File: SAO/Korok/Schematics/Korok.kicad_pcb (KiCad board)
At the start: 2 copper layers, 44.5 x 76.5 mm, 7 parts, among them J2 Debug, J3 Conn_02x03_Odd_Even, SW1 SW_SPDT, U1 CH32V006, U4 W25Q16JVSS

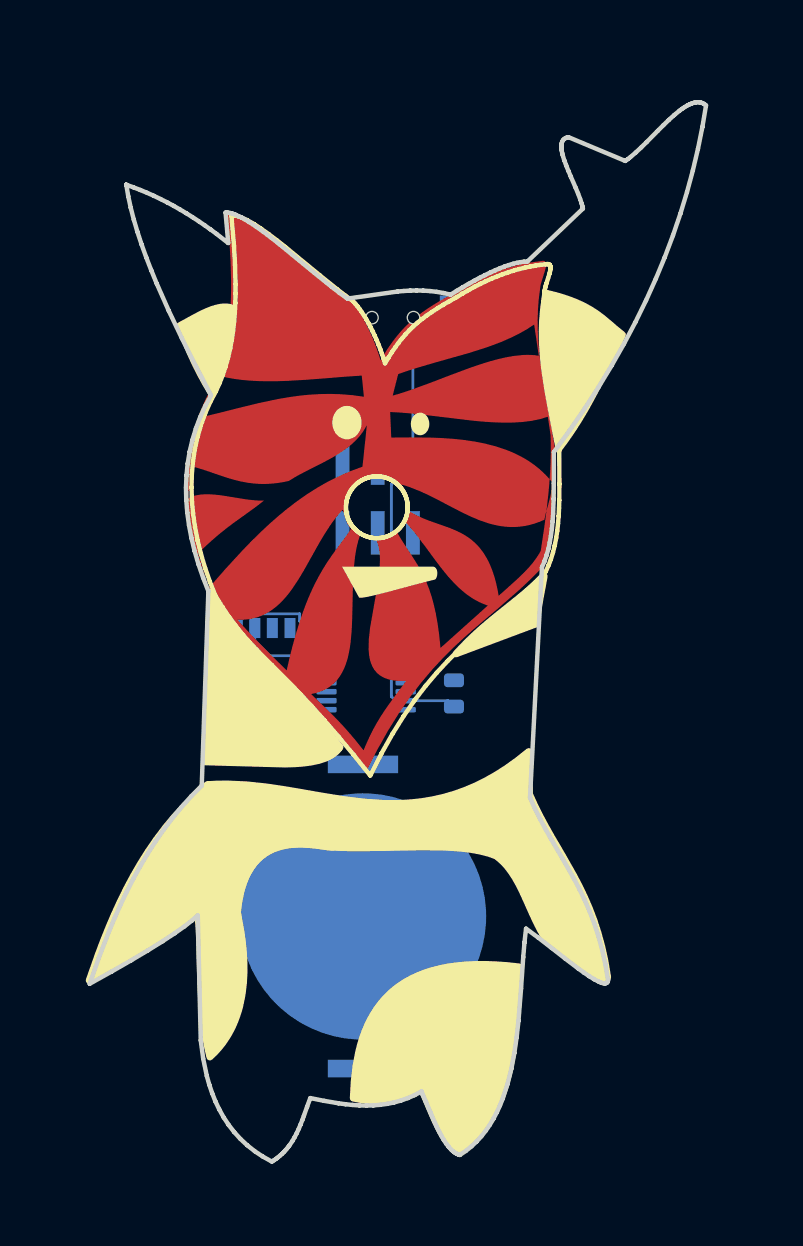
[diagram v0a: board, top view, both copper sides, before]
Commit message: Finished korok and toplight
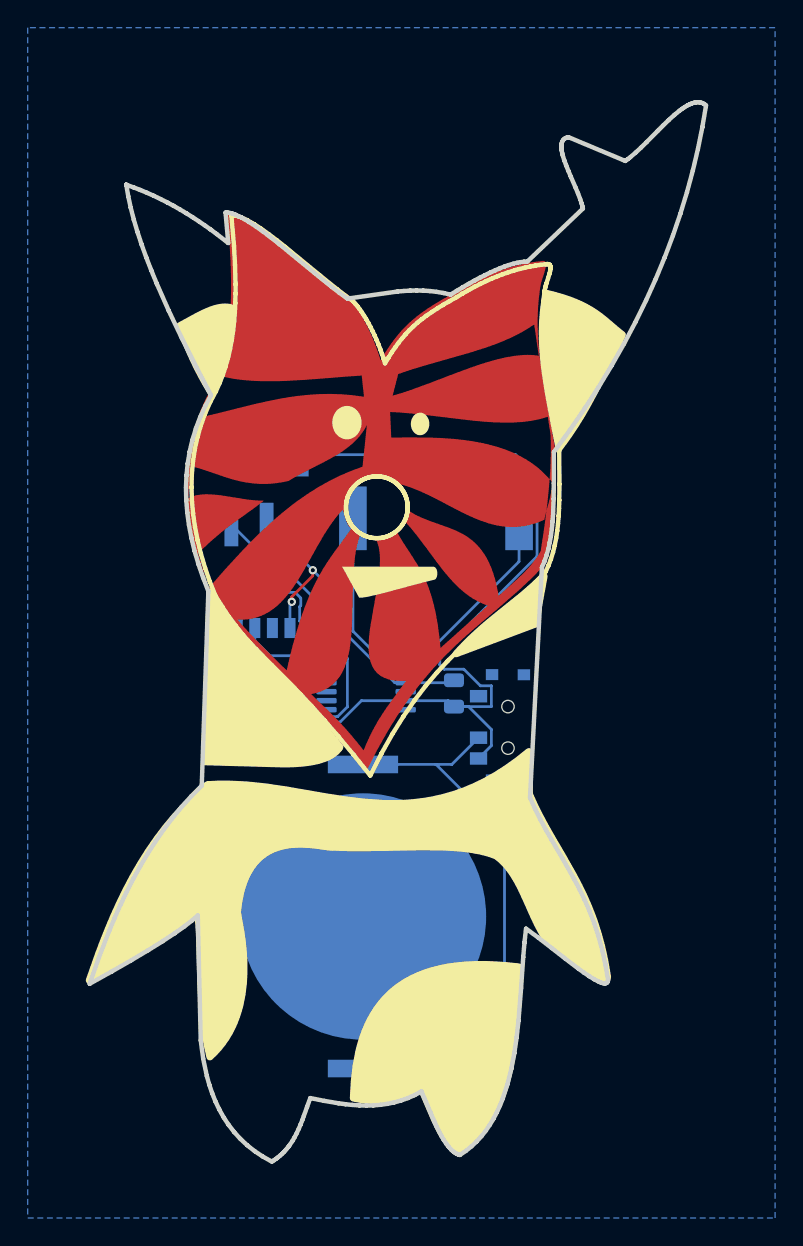
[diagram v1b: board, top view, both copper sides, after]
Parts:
- added J1: Speaker, UE_Buzzer:Fuet-1230, B.Cu at (161.5, 78.5)
- moved SW1 30.7 mm to (166.7, 93.5), turned to 90 degrees
- moved J3 8.05 mm to (149.3, 76.4)
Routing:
- net Net-(BT1-+): track 0.00 -> 39.9 mm
- net +3V3: track 31.0 -> 69.4 mm
- net SWIO: track 0.00 -> 25.4 mm
- net GND: track 0.00 -> 23.4 mm, vias 0 -> 2
- net PA1: track 0.00 -> 14.4 mm
- net PA2: track 0.00 -> 13.2 mm
- net PD2: track 8.07 -> 10.4 mm
- added copper zone on B.Cu, net GND
